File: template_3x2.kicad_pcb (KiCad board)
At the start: 2 copper layers, 0 parts

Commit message: Completed version 1.0.
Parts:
- added MDB1: MODULAR_DEVICE_BASE_3X2_MALE, template_3x2:MODULAR_DEVICE_BASE_3X2_MALE, F.Cu at (107.3, 88.9)
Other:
- board outline added: 69.8 x 40.6 mm
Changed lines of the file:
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@@
     (links 0)
     (no_connects 0)
-    (area 93.230699 75.196699 211.569301 130.543301)
+    (area 0 0 0 0)
     (thickness 1.6)
-    (drawings 2)
+    (drawings 6)
     (tracks 0)
     (zones 0)
-    (modules 0)
+    (modules 1)
     (nets 1)
   )
@@
     (47 F.CrtYd user)
     (48 B.Fab user)
-    (49 F.Fab user)
+    (49 F.Fab user hide)
   )
   (setup
@@
     (diff_pair_width 0.254)
   )
-  (gr_text https://github.com/janelia-modular-devices (at 100.33 118.11) (layer F.SilkS)
+  (module template_3x2:MODULAR_DEVICE_BASE_3X2_MALE (layer F.Cu)
+    (at 107.315 88.9)
+    (fp_text reference MDB1 (at 0 0) (layer F.SilkS) hide
+      (effects (font (size 1.016 1.016) (thickness 0.254)))
+    )
+    (fp_text value MODULAR_DEVICE_BASE_3X2_MALE (at 0 2.54) (layer F.SilkS) hide
+      (effects (font (thickness 0.3048)))
+    )
+    (fp_circle (center -17.78 -12.7) (end -15.24 -12.7) (layer F.SilkS) (width 0.2286))
+    (fp_circle (center -17.78 12.7) (end -15.24 12.7) (layer F.SilkS) (width 0.2286))
+    (fp_circle (center 22.86 17.78) (end 25.4 17.78) (layer F.SilkS) (width 0.2286))
+    (fp_circle (center 22.86 -17.78) (end 25.4 -17.78) (layer F.SilkS) (width 0.2286))
+    (fp_line (start -20.32 16.51) (end -20.32 19.05) (layer B.SilkS) (width 0.381))
+    (fp_line (start -20.32 19.05) (end 20.32 19.05) (layer B.SilkS) (width 0.381))
+    (fp_line (start 20.32 19.05) (end 20.32 16.51) (layer B.SilkS) (width 0.381))
+    (fp_line (start 20.32 16.51) (end -20.32 16.51) (layer B.SilkS) (width 0.381))
+    (fp_line (start -20.32 -19.05) (end -20.32 -16.51) (layer B.SilkS) (width 0.381))
+    (fp_line (start -20.32 -16.51) (end 20.32 -16.51) (layer B.SilkS) (width 0.381))
+    (fp_line (start 20.32 -16.51) (end 20.32 -19.05) (layer B.SilkS) (width 0.381))
+    (fp_line (start 20.32 -19.05) (end -20.32 -19.05) (layer B.SilkS) (width 0.381))
+    (fp_line (start -21.59 -20.32) (end -21.59 20.32) (layer F.Fab) (width 0.2286))
+    (fp_line (start -21.59 20.32) (end 48.26 20.32) (layer F.Fab) (width 0.2286))
+    (fp_line (start 48.26 20.32) (end 48.26 -20.32) (layer F.Fab) (width 0.2286))
+    (fp_line (start 48.26 -20.32) (end -21.59 -20.32) (layer F.Fab) (width 0.2286))
+    (pad GND thru_hole oval (at -16.51 -17.78) (size 1.8542 2.54) (drill 1.0922) (layers *.Cu *.Mask))
+    (pad 24 thru_hole oval (at -13.97 -17.78) (size 1.8542 2.54) (drill 1.0922) (layers *.Cu *.Mask))
+    (pad VDD thru_hole rect (at -19.05 -17.78) (size 1.8542 2.54) (drill 1.0922) (layers *.Cu *.Mask))
+    (pad 25 thru_hole oval (at -11.43 -17.78) (size 1.8542 2.54) (drill 1.0922) (layers *.Cu *.Mask))
+    (pad 2 thru_hole oval (at -8.89 -17.78) (size 1.8542 2.54) (drill 1.0922) (layers *.Cu *.Mask))
+    (pad 3 thru_hole oval (at -6.35 -17.78) (size 1.8542 2.54) (drill 1.0922) (layers *.Cu *.Mask))
+    (pad 4 thru_hole oval (at -3.81 -17.78) (size 1.8542 2.54) (drill 1.0922) (layers *.Cu *.Mask))
+    (pad 5 thru_hole oval (at -1.27 -17.78) (size 1.8542 2.54) (drill 1.0922) (layers *.Cu *.Mask))
+    (pad 6 thru_hole oval (at 1.27 -17.78) (size 1.8542 2.54) (drill 1.0922) (layers *.Cu *.Mask))
+    (pad 30 thru_hole oval (at 3.81 -17.78) (size 1.8542 2.54) (drill 1.0922) (layers *.Cu *.Mask))
+    (pad 29 thru_hole oval (at 6.35 -17.78) (size 1.8542 2.54) (drill 1.0922) (layers *.Cu *.Mask))
+    (pad 9 thru_hole oval (at 8.89 -17.78) (size 1.8542 2.54) (drill 1.0922) (layers *.Cu *.Mask))
+    (pad 10 thru_hole oval (at 11.43 -17.78) (size 1.8542 2.54) (drill 1.0922) (layers *.Cu *.Mask))
+    (pad 11 thru_hole oval (at 13.97 -17.78) (size 1.8542 2.54) (drill 1.0922) (layers *.Cu *.Mask))
+    (pad 12 thru_hole oval (at 16.51 -17.78) (size 1.8542 2.54) (drill 1.0922) (layers *.Cu *.Mask))
+    (pad 28 thru_hole oval (at 19.05 -17.78) (size 1.8542 2.54) (drill 1.0922) (layers *.Cu *.Mask))
+    (pad DAC thru_hole oval (at 19.05 17.78) (size 1.8542 2.54) (drill 1.0922) (layers *.Cu *.Mask))
+    (pad 13 thru_hole oval (at 16.51 17.78) (size 1.8542 2.54) (drill 1.0922) (layers *.Cu *.Mask))
+    (pad 14 thru_hole oval (at 13.97 17.78) (size 1.8542 2.54) (drill 1.0922) (layers *.Cu *.Mask))
+    (pad 15 thru_hole oval (at 11.43 17.78) (size 1.8542 2.54) (drill 1.0922) (layers *.Cu *.Mask))
+    (pad 16 thru_hole oval (at 8.89 17.78) (size 1.8542 2.54) (drill 1.0922) (layers *.Cu *.Mask))
+    (pad 17 thru_hole oval (at 6.35 17.78) (size 1.8542 2.54) (drill 1.0922) (layers *.Cu *.Mask))
+    (pad 18 thru_hole oval (at 3.81 17.78) (size 1.8542 2.54) (drill 1.0922) (layers *.Cu *.Mask))
+    (pad 19 thru_hole oval (at 1.27 17.78) (size 1.8542 2.54) (drill 1.0922) (layers *.Cu *.Mask))
+    (pad 20 thru_hole oval (at -1.27 17.78) (size 1.8542 2.54) (drill 1.0922) (layers *.Cu *.Mask))
+    (pad 21 thru_hole oval (at -3.81 17.78) (size 1.8542 2.54) (drill 1.0922) (layers *.Cu *.Mask))
+    (pad 22 thru_hole oval (at -6.35 17.78) (size 1.8542 2.54) (drill 1.0922) (layers *.Cu *.Mask))
+    (pad 23 thru_hole oval (at -8.89 17.78) (size 1.8542 2.54) (drill 1.0922) (layers *.Cu *.Mask))
+    (pad 3V3 thru_hole oval (at -11.43 17.78) (size 1.8542 2.54) (drill 1.0922) (layers *.Cu *.Mask))
+    (pad AGND thru_hole oval (at -13.97 17.78) (size 1.8542 2.54) (drill 1.0922) (layers *.Cu *.Mask))
+    (pad VEE thru_hole oval (at -16.51 17.78) (size 1.8542 2.54) (drill 1.0922) (layers *.Cu *.Mask))
+    (pad AREF thru_hole oval (at -19.05 17.78) (size 1.8542 2.54) (drill 1.0922) (layers *.Cu *.Mask))
+    (pad "" thru_hole circle (at -17.78 -12.7) (size 3.556 3.556) (drill 3.302) (layers *.Cu *.Mask F.SilkS))
+    (pad "" thru_hole circle (at -17.78 12.7) (size 3.556 3.556) (drill 3.302) (layers *.Cu *.Mask F.SilkS))
+    (pad "" thru_hole circle (at 22.86 17.78) (size 3.556 3.556) (drill 3.302) (layers *.Cu *.Mask F.SilkS))
+    (pad "" thru_hole circle (at 22.86 -17.78) (size 3.556 3.556) (drill 3.302) (layers *.Cu *.Mask F.SilkS))
+  )
+  (gr_line (start 155.575 68.58) (end 85.725 68.58) (angle 90) (layer Edge.Cuts) (width 0.2286))
+  (gr_line (start 155.575 109.22) (end 155.575 68.58) (angle 90) (layer Edge.Cuts) (width 0.2286))
+  (gr_line (start 85.725 109.22) (end 155.575 109.22) (angle 90) (layer Edge.Cuts) (width 0.2286))
+  (gr_line (start 85.725 68.58) (end 85.725 109.22) (angle 90) (layer Edge.Cuts) (width 0.2286))
+  (gr_text https://github.com/janelia-modular-devices (at 109.855 104.14) (layer F.SilkS)
     (effects (font (size 1.016 1.016) (thickness 0.1905)))
   )
-  (gr_text "Janelia Modular Device\ntemplate\npart_number: 1000\n02/2017 ver 1.0\n3x2" (at 93.98 125.73) (layer F.SilkS)
-    (effects (font (size 1.016 1.016) (thickness 0.254)) (justify left))
+  (gr_text "Janelia Modular Device\ntemplate\npart_number: 1000\n02/2017 ver 1.0 3x2" (at 89.535 88.9 90) (layer F.SilkS)
+    (effects (font (size 1.016 1.016) (thickness 0.254)))
   )
 )

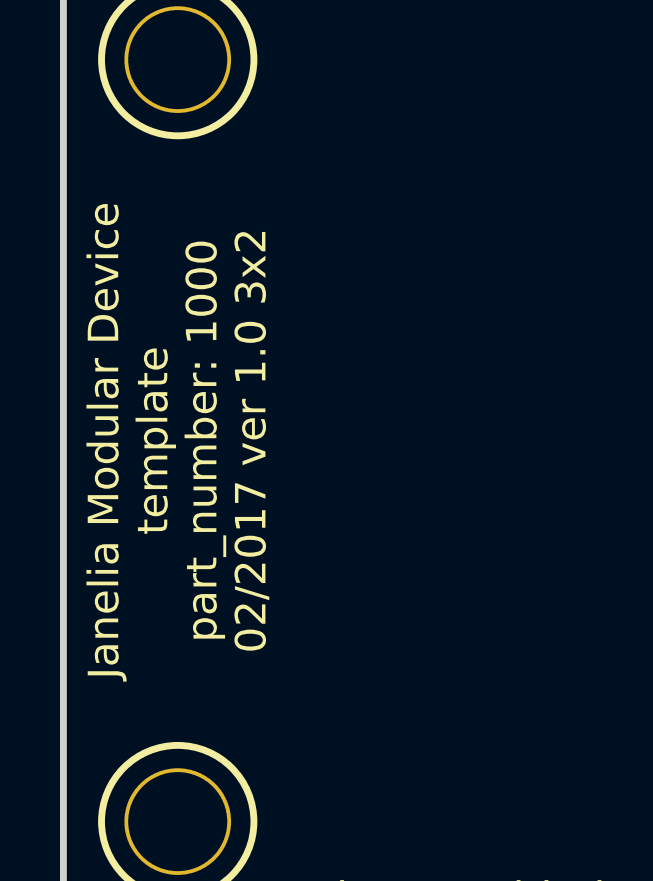
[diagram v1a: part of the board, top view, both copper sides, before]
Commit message: Updated default part number.
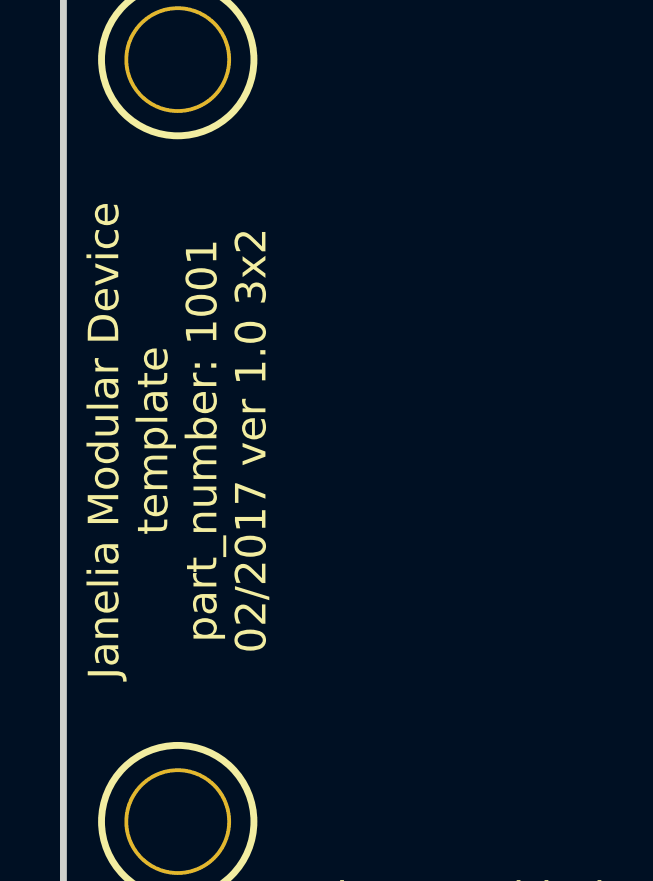
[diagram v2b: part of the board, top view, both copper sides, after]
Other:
- board text added: "Janelia Modular Device template part_number: 1001 02/2017 ver 1.0 3x2"
- board text removed: "Janelia Modular Device template part_number: 1000 02/2017 ver 1.0 3x2"
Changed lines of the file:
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@@
-(kicad_pcb (version 20170123) (host pcbnew no-vcs-found-7602~57~ubuntu16.04.1)
+(kicad_pcb (version 20170123) (host pcbnew no-vcs-found-ea855c1~58~ubuntu16.04.1)
   (general
     (links 0)
     (no_connects 0)
-    (area 0 0 0 0)
+    (area 85.356699 68.211699 155.943301 109.588301)
     (thickness 1.6)
     (drawings 6)
@@
     (effects (font (size 1.016 1.016) (thickness 0.1905)))
   )
-  (gr_text "Janelia Modular Device\ntemplate\npart_number: 1000\n02/2017 ver 1.0 3x2" (at 89.535 88.9 90) (layer F.SilkS)
+  (gr_text "Janelia Modular Device\ntemplate\npart_number: 1001\n02/2017 ver 1.0 3x2" (at 89.535 88.9 90) (layer F.SilkS)
     (effects (font (size 1.016 1.016) (thickness 0.254)))
   )

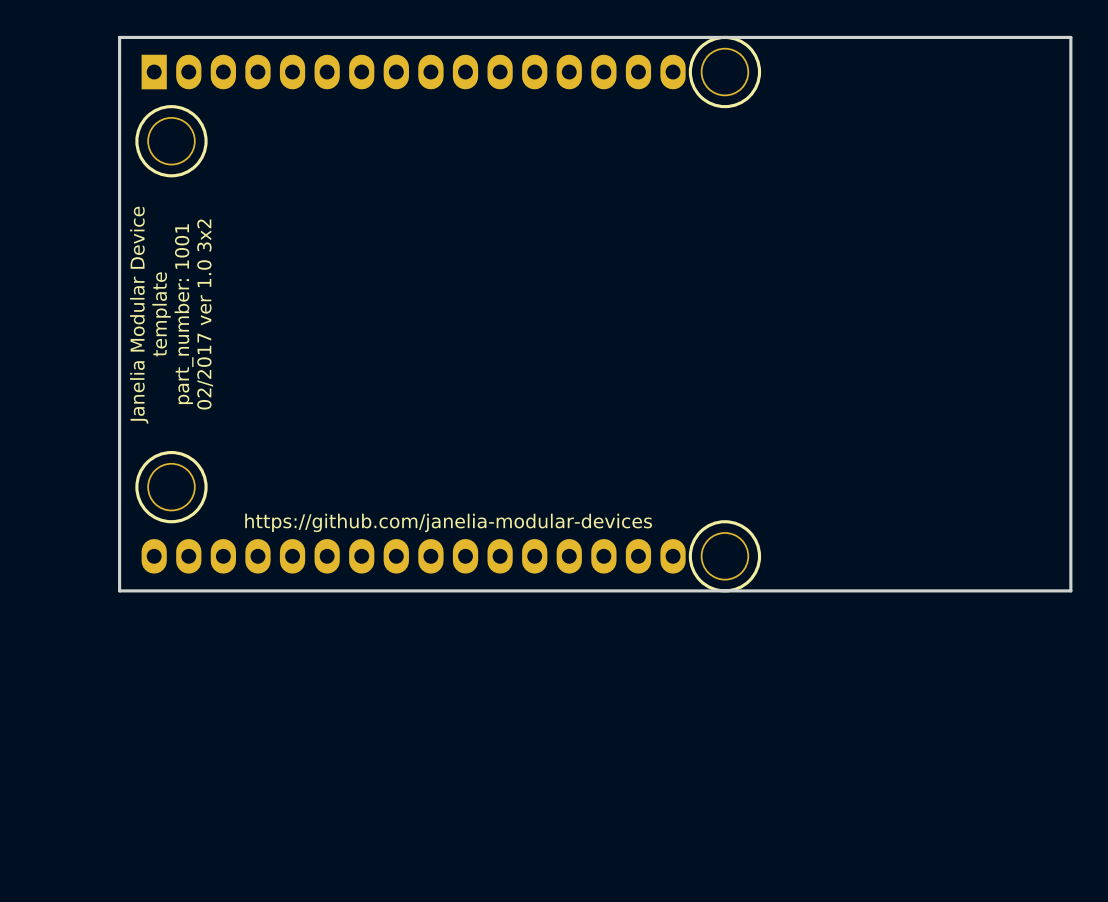
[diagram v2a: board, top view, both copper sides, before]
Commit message: Updated edge positions.
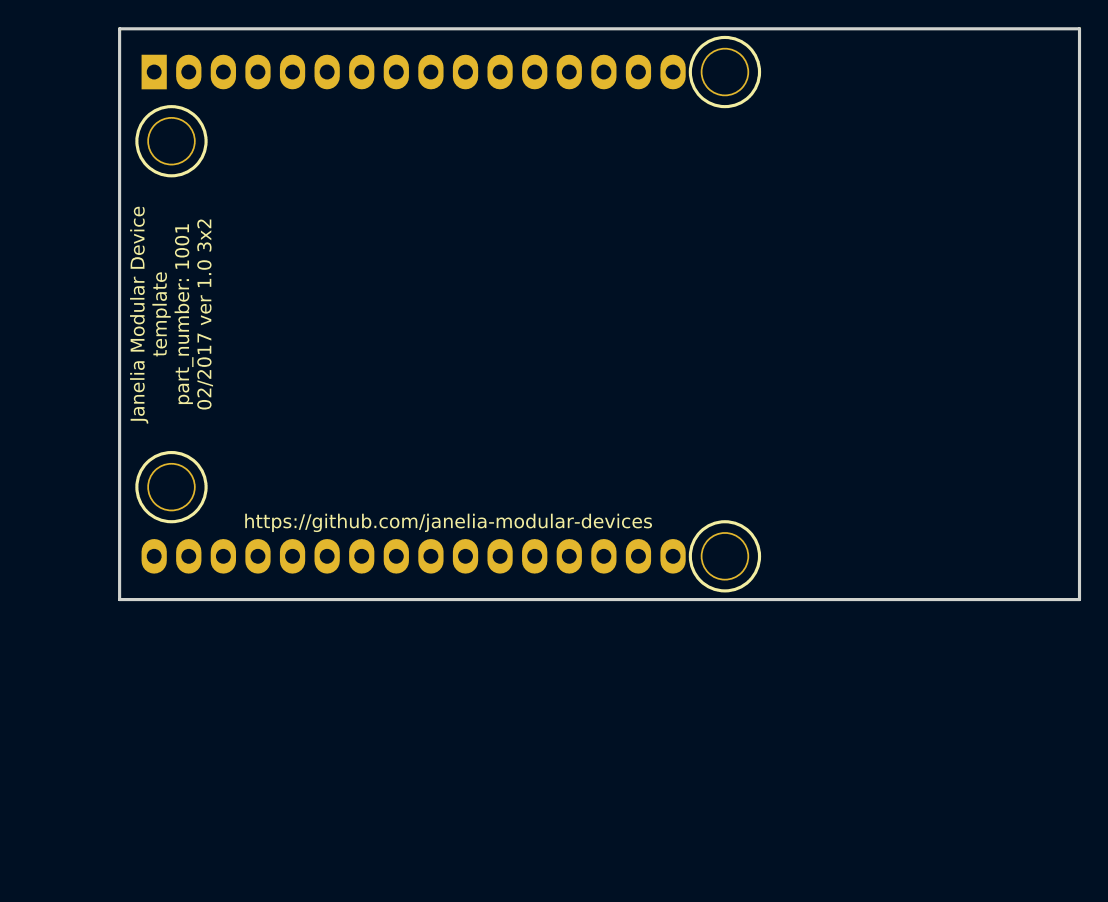
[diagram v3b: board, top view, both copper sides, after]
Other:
- board size 69.8 x 40.6 mm -> 70.5 x 41.9 mm

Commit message: Updated footprints on board.
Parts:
- MDB1: value MODULAR_DEVICE_BASE_3X2_MALE -> VAL**
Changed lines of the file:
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@@
-(kicad_pcb (version 20170123) (host pcbnew no-vcs-found-0633d90~59~ubuntu16.04.1)
+(kicad_pcb (version 20171130) (host pcbnew 6.0.0-rc1-unknown-4d73cfb~66~ubuntu18.04.1)
   (general
     (thickness 1.6)
@@
     (zone_45_only no)
     (trace_min 0.254)
-    (segment_width 0.2286)
-    (edge_width 0.2286)
     (via_size 0.889)
     (via_drill 0.635)
@@
     (uvia_min_size 0.508)
     (uvia_min_drill 0.127)
+    (edge_width 0.2286)
+    (segment_width 0.2286)
     (pcb_text_width 0.3)
     (pcb_text_size 1.5 1.5)
@@
     (pad_drill 0)
     (pad_to_mask_clearance 0)
+    (solder_mask_min_width 0.25)
     (aux_axis_origin 0 0)
     (visible_elements FFFFF77F)
@@
       (layerselection 0x000f0_ffffffff)
       (usegerberextensions true)
+      (usegerberattributes false)
+      (usegerberadvancedattributes false)
+      (creategerberjobfile false)
       (excludeedgelayer false)
       (linewidth 0.100000)
@@
       (hpglpennumber 1)
       (hpglpenspeed 20)
-      (hpglpendiameter 15)
+      (hpglpendiameter 15.000000)
       (psnegative false)
       (psa4output false)
@@
       (drillshape 0)
       (scaleselection 1)
-      (outputdirectory gerbers/))
+      (outputdirectory "gerbers/"))
   )
   (net 0 "")
@@
     (uvia_dia 0.508)
     (uvia_drill 0.127)
+    (diff_pair_width 0.254)
     (diff_pair_gap 0.254)
-    (diff_pair_width 0.254)
   )
   (net_class GND ""
@@
     (uvia_dia 0.508)
     (uvia_drill 0.127)
+    (diff_pair_width 0.254)
     (diff_pair_gap 0.254)
-    (diff_pair_width 0.254)
   )
   (net_class LEDPOWER ""
@@
     (uvia_dia 0.508)
     (uvia_drill 0.127)
+    (diff_pair_width 0.254)
     (diff_pair_gap 0.254)
-    (diff_pair_width 0.254)
   )
   (net_class POWER ""
@@
     (uvia_dia 0.508)
     (uvia_drill 0.127)
+    (diff_pair_width 0.254)
     (diff_pair_gap 0.254)
-    (diff_pair_width 0.254)
   )
   (net_class SIGNAL ""
@@
     (uvia_dia 0.508)
     (uvia_drill 0.127)
+    (diff_pair_width 0.254)
     (diff_pair_gap 0.254)
-    (diff_pair_width 0.254)
   )
   (net_class SUPERPOWER ""
@@
     (uvia_dia 0.508)
     (uvia_drill 0.127)
+    (diff_pair_width 0.254)
     (diff_pair_gap 0.254)
-    (diff_pair_width 0.254)
   )
   (module template_3x2:MODULAR_DEVICE_BASE_3X2_MALE (layer F.Cu)
@@
       (effects (font (size 1.016 1.016) (thickness 0.254)))
     )
-    (fp_text value MODULAR_DEVICE_BASE_3X2_MALE (at 0 2.54) (layer F.SilkS) hide
-      (effects (font (thickness 0.3048)))
+    (fp_text value VAL** (at 0 2.54) (layer F.SilkS) hide
+      (effects (font (size 1.524 1.524) (thickness 0.3048)))
     )
     (fp_line (start 48.895 -20.955) (end -21.59 -20.955) (layer F.Fab) (width 0.2286))
@@
     (fp_circle (center -17.78 12.7) (end -15.24 12.7) (layer F.SilkS) (width 0.2286))
     (fp_circle (center -17.78 -12.7) (end -15.24 -12.7) (layer F.SilkS) (width 0.2286))
-    (pad "" thru_hole circle (at 22.86 -17.78) (size 3.556 3.556) (drill 3.302) (layers *.Cu *.Mask F.SilkS))
-    (pad "" thru_hole circle (at 22.86 17.78) (size 3.556 3.556) (drill 3.302) (layers *.Cu *.Mask F.SilkS))
-    (pad "" thru_hole circle (at -17.78 12.7) (size 3.556 3.556) (drill 3.302) (layers *.Cu *.Mask F.SilkS))
-    (pad "" thru_hole circle (at -17.78 -12.7) (size 3.556 3.556) (drill 3.302) (layers *.Cu *.Mask F.SilkS))
+    (pad "" thru_hole circle (at 22.86 -17.78) (size 3.556 3.556) (drill 3.302) (layers *.Cu *.Mask))
+    (pad "" thru_hole circle (at 22.86 17.78) (size 3.556 3.556) (drill 3.302) (layers *.Cu *.Mask))
+    (pad "" thru_hole circle (at -17.78 12.7) (size 3.556 3.556) (drill 3.302) (layers *.Cu *.Mask))
+    (pad "" thru_hole circle (at -17.78 -12.7) (size 3.556 3.556) (drill 3.302) (layers *.Cu *.Mask))
     (pad AREF thru_hole oval (at -19.05 17.78) (size 1.8542 2.54) (drill 1.0922) (layers *.Cu *.Mask))
     (pad VEE thru_hole oval (at -16.51 17.78) (size 1.8542 2.54) (drill 1.0922) (layers *.Cu *.Mask))
